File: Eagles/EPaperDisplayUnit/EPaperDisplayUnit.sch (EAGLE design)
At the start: 99 parts, among them IC1 AT25, J26 SOLDER_JUMPER_2WAY-TRACE12, J27 SOLDER_JUMPER_2WAY-TRACE12, U2 LPC824M201JHI33, X1 32.768kHz, X2 FH12-50S-0.5SH

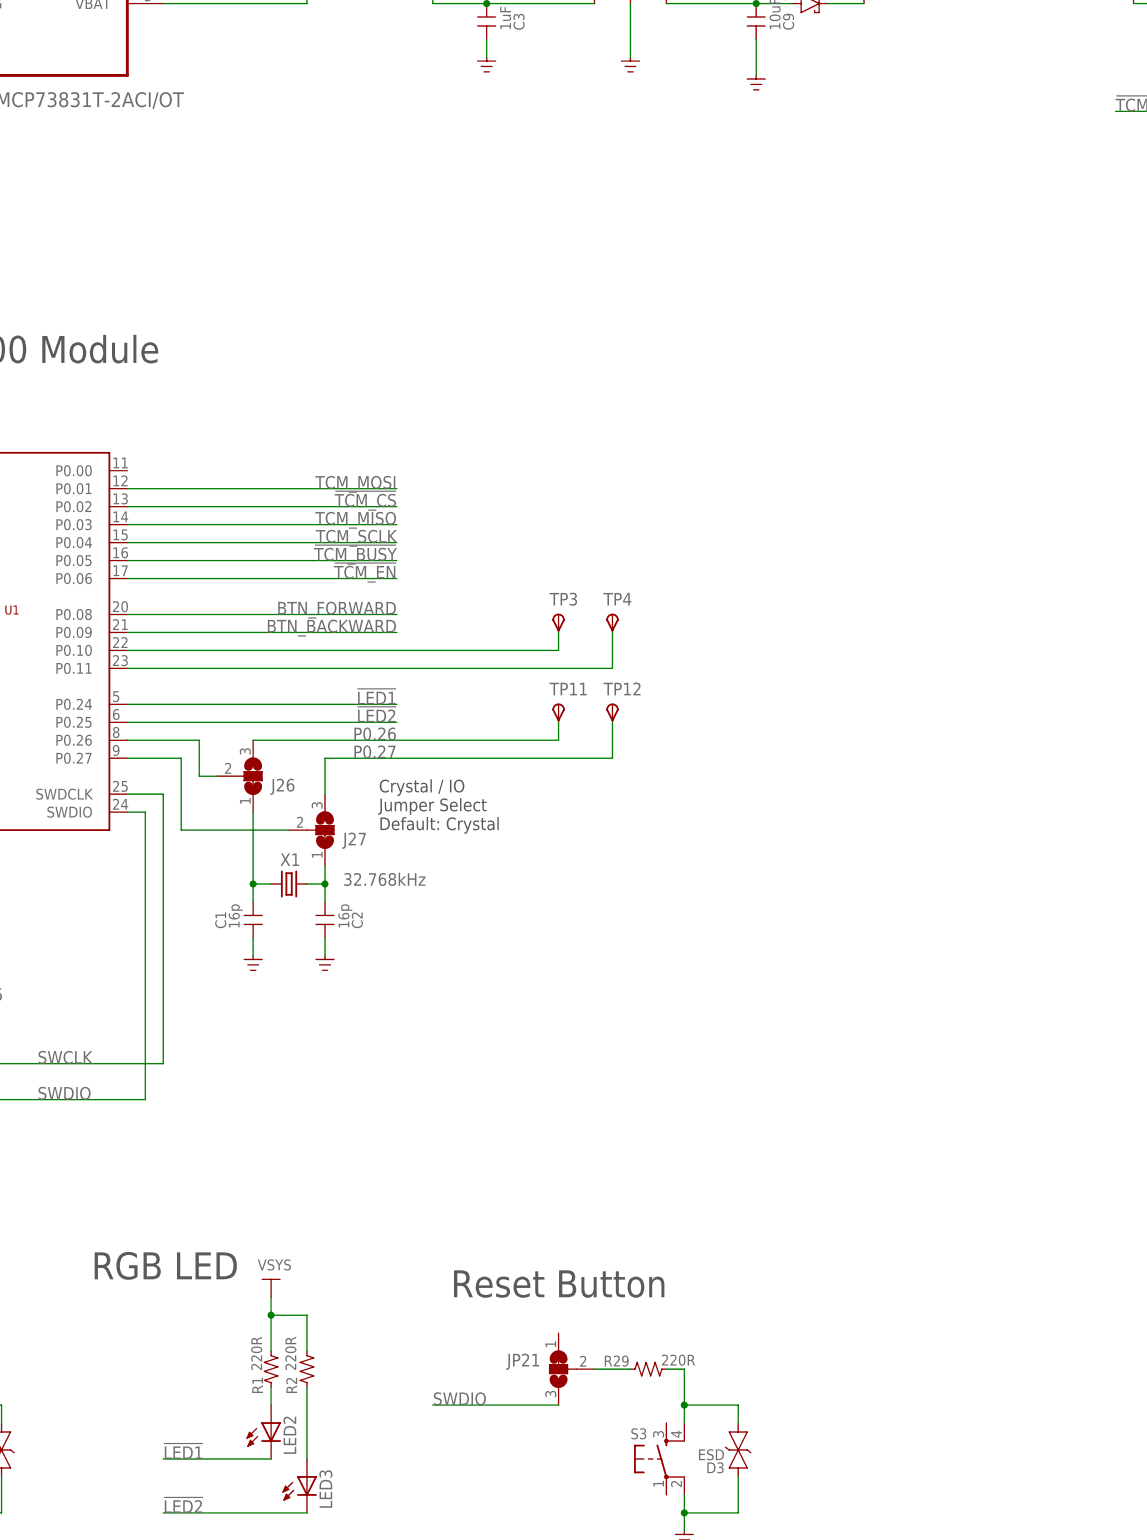
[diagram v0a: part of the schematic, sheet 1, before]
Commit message: [Draw schematic for the display unit #8]
Add a hirose USB connector for charging
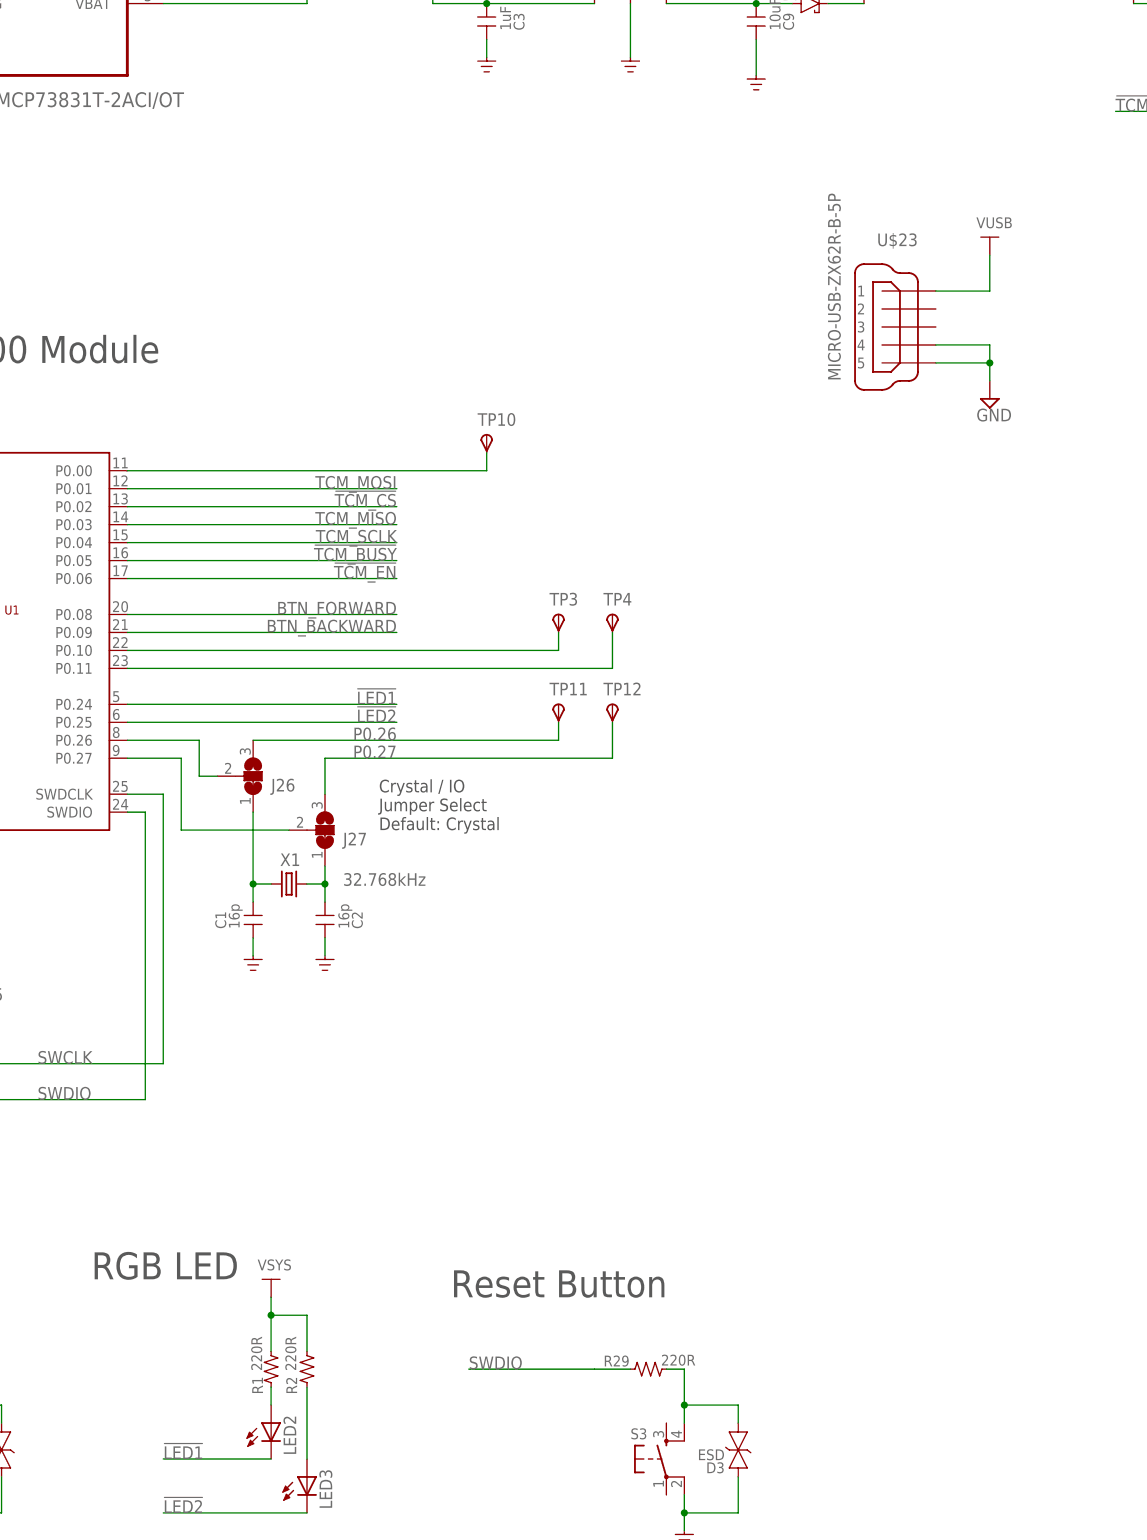
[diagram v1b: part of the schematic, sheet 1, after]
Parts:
- removed JP21: SOLDER_JUMPER_2WAY-TRACE12, rigado-connectors:SOLDER_JUMPER_2WAY-TRACE12
- added TP10: TPSPAD1-13Y, testpad:TPSPAD1-13Y
- added U$23: MICRO-USB-ZX62R-B-5P, con-hirose:MICRO-USB-ZX62R-B-5P
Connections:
- new net N$1: TP10.PP, U1.P0.00
- net 5V0: now also U$23.1
- net GND: now also U$23.4, U$23.5
- net N$48: no longer JP21.2
- net SWDIO: no longer JP21.3
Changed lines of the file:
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@@
 <attribute name="VPN" value="1276-4360-1-ND"/>
 </part>
-<part name="JP21" library="rigado-connectors" deviceset="SOLDER_JUMPER_2WAY" device="-TRACE12"/>
 <part name="FID2" library="rigado-pcb" deviceset="FIDUCIAL" device="-.04" value="FIDUCIAL-.04"/>
 <part name="FID4" library="rigado-pcb" deviceset="FIDUCIAL" device="-.04" value="FIDUCIAL-.04"/>
@@
 <part name="TP11" library="testpad" deviceset="TPS" device="PAD1-13Y"/>
 <part name="TP12" library="testpad" deviceset="TPS" device="PAD1-13Y"/>
+<part name="TP10" library="testpad" deviceset="TPS" device="PAD1-13Y"/>
+<part name="U$23" library="con-hirose" deviceset="MICRO-USB-" device="ZX62R-B-5P"/>
+<part name="U$24" library="supply" deviceset="VUSB" device=""/>
+<part name="SUPPLY7" library="supply2" deviceset="GND" device=""/>
 </parts>
 <sheets>
@@
 <text x="68.58" y="68.58" size="3.81" layer="97">RGB LED</text>
 <text x="22.86" y="68.58" size="3.81" layer="97">User Buttons</text>
-<wire x1="134.62" y1="58.42" x2="134.62" y2="55.88" width="0.1524" layer="94"/>
 <text x="119.38" y="66.04" size="3.81" layer="97">Reset Button</text>
 </plain>
@@
 <attribute name="FIRE" x="147.32" y="55.88" size="1.778" layer="96" rot="R90" display="off"/>
 <attribute name="CRITICAL" x="147.32" y="55.88" size="1.778" layer="96" rot="R90" display="off"/>
-</instance>
-<instance part="JP21" gate="1" x="134.62" y="55.88" smashed="yes" rot="MR0">
-<attribute name="NAME" x="132.08" y="56.261" size="1.778" layer="95" rot="MR0"/>
 </instance>
 <instance part="FID2" gate="G$1" x="411.48" y="50.8"/>
@@
 <instance part="TP11" gate="G$1" x="134.62" y="149.86"/>
 <instance part="TP12" gate="G$1" x="142.24" y="149.86"/>
+<instance part="TP10" gate="G$1" x="124.46" y="187.96"/>
+<instance part="U$23" gate="G$1" x="182.88" y="203.2" rot="MR0"/>
+<instance part="U$24" gate="G$1" x="195.58" y="215.9"/>
+<instance part="SUPPLY7" gate="GND" x="195.58" y="193.04"/>
 </instances>
 <busses>
@@
 <wire x1="40.64" y1="104.14" x2="40.64" y2="91.44" width="0.1524" layer="91"/>
 </segment>
+<segment>
+<pinref part="U$23" gate="G$1" pin="4"/>
+<pinref part="SUPPLY7" gate="GND" pin="GND"/>
+<wire x1="187.96" y1="200.66" x2="195.58" y2="200.66" width="0.1524" layer="91"/>
+<wire x1="195.58" y1="200.66" x2="195.58" y2="198.12" width="0.1524" layer="91"/>
+<pinref part="U$23" gate="G$1" pin="5"/>
+<wire x1="195.58" y1="198.12" x2="195.58" y2="195.58" width="0.1524" layer="91"/>
+<wire x1="187.96" y1="198.12" x2="195.58" y2="198.12" width="0.1524" layer="91"/>
+<junction x="195.58" y="198.12"/>
+</segment>
 </net>
 <net name="SWCLK" class="0">
@@
 <wire x1="30.48" y1="266.7" x2="76.2" y2="266.7" width="0.1524" layer="91"/>
 </segment>
+<segment>
+<pinref part="U$24" gate="G$1" pin="5V0"/>
+<wire x1="195.58" y1="213.36" x2="195.58" y2="208.28" width="0.1524" layer="91"/>
+<pinref part="U$23" gate="G$1" pin="1"/>
+<wire x1="195.58" y1="208.28" x2="187.96" y2="208.28" width="0.1524" layer="91"/>
+</segment>
 </net>
 <net name="!TCM_EN" class="0">
@@
 </segment>
 <segment>
-<pinref part="JP21" gate="1" pin="3"/>
-<wire x1="134.62" y1="50.8" x2="116.84" y2="50.8" width="0.1524" layer="91"/>
-<label x="116.84" y="50.8" size="1.778" layer="95"/>
+<wire x1="139.7" y1="55.88" x2="121.92" y2="55.88" width="0.1524" layer="91"/>
+<label x="121.92" y="55.88" size="1.778" layer="95"/>
 </segment>
 </net>
@@
 <segment>
 <pinref part="R29" gate="G$1" pin="1"/>
-<pinref part="JP21" gate="1" pin="2"/>
 <wire x1="144.78" y1="55.88" x2="139.7" y2="55.88" width="0.1524" layer="91"/>
 </segment>
@@
 </segment>
 </net>
+<net name="N$1" class="0">
+<segment>
+<pinref part="U1" gate="A" pin="P0.00"/>
+<pinref part="TP10" gate="G$1" pin="PP"/>
+<wire x1="73.66" y1="182.88" x2="124.46" y2="182.88" width="0.1524" layer="91"/>
+<wire x1="124.46" y1="182.88" x2="124.46" y2="185.42" width="0.1524" layer="91"/>
+</segment>
+</net>
